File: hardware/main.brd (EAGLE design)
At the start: 95.2 x 80.4 mm, 100 parts, among them IC1 MPU-6050, IC2 TB6612FNG, M1 MOTOR_MOUNT_V2, M2 LED_MOUNT, M3 LED_MOUNT, M4 LED_MOUNT, M5 LED_MOUNT, M6 LED_MOUNT, M7 LED_MOUNT, Q7 IRLML2244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

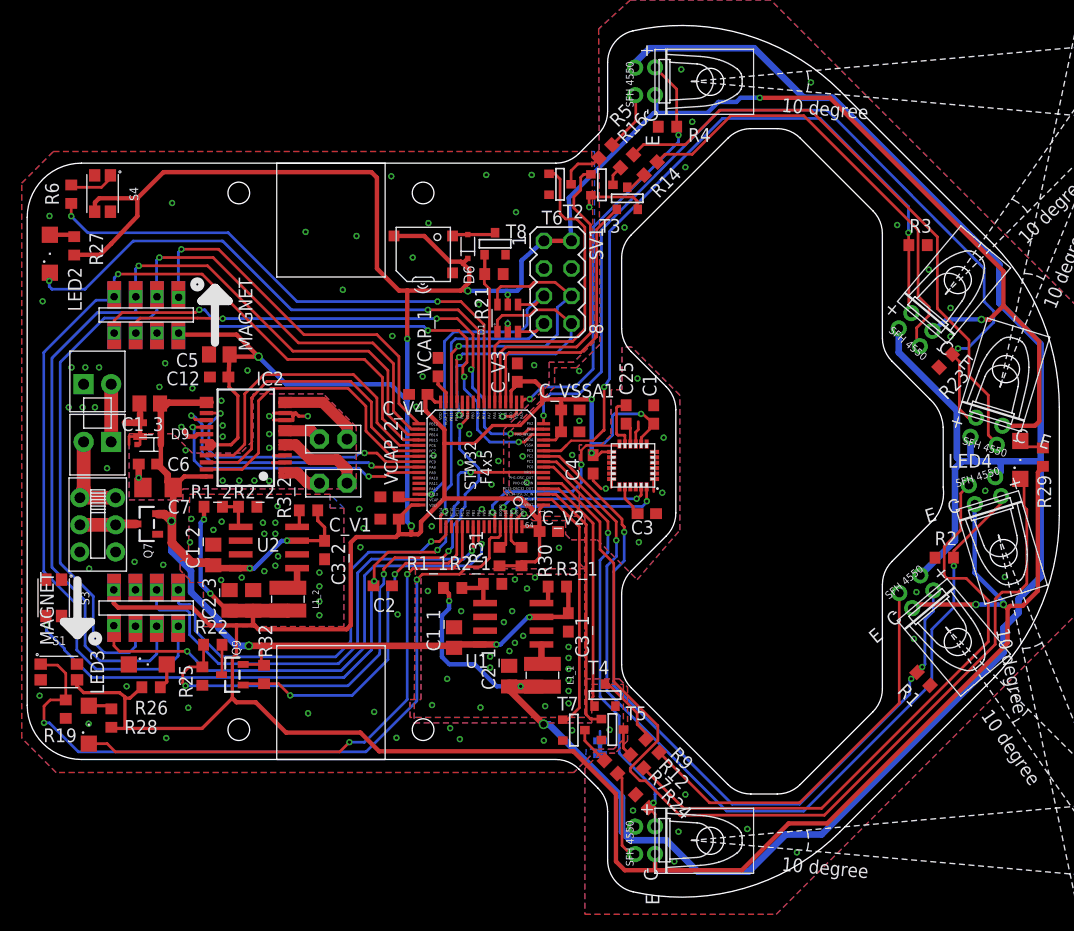
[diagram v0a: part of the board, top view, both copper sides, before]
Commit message: fixed boot0 button, buzzer footprint, togh matches 3d model
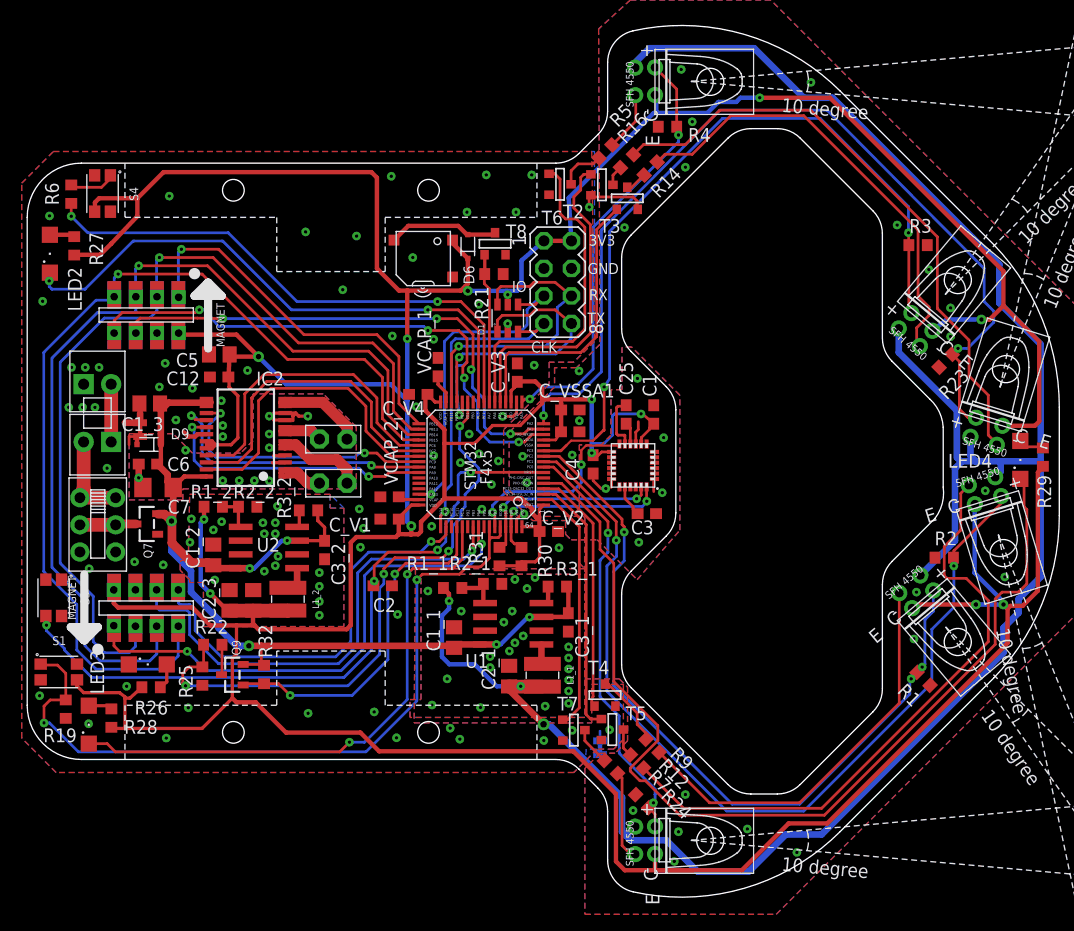
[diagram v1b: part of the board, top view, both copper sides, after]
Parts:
- moved SPK1 0.38 mm to (36.5, 18.7)
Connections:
- net +3V3: now also SPK1.+; no longer SPK1.-
- net BOOT0: now also U3.PB6
- net N$30: now also SPK1.-; no longer SPK1.+
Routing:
- net N$30: track 4.05 -> 10.3 mm
- net +3V3: track 527.2 -> 521.6 mm
- net BOOT0: track 68.7 -> 69.9 mm
- net GND: track 35.9 -> 35.3 mm, vias 111 -> 110
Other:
- board text added: "3V3"
- board text added: "CLK"
- board text added: "GND"
- board text added: "IO"
- board text added: "RX"
- board text added: "TX"

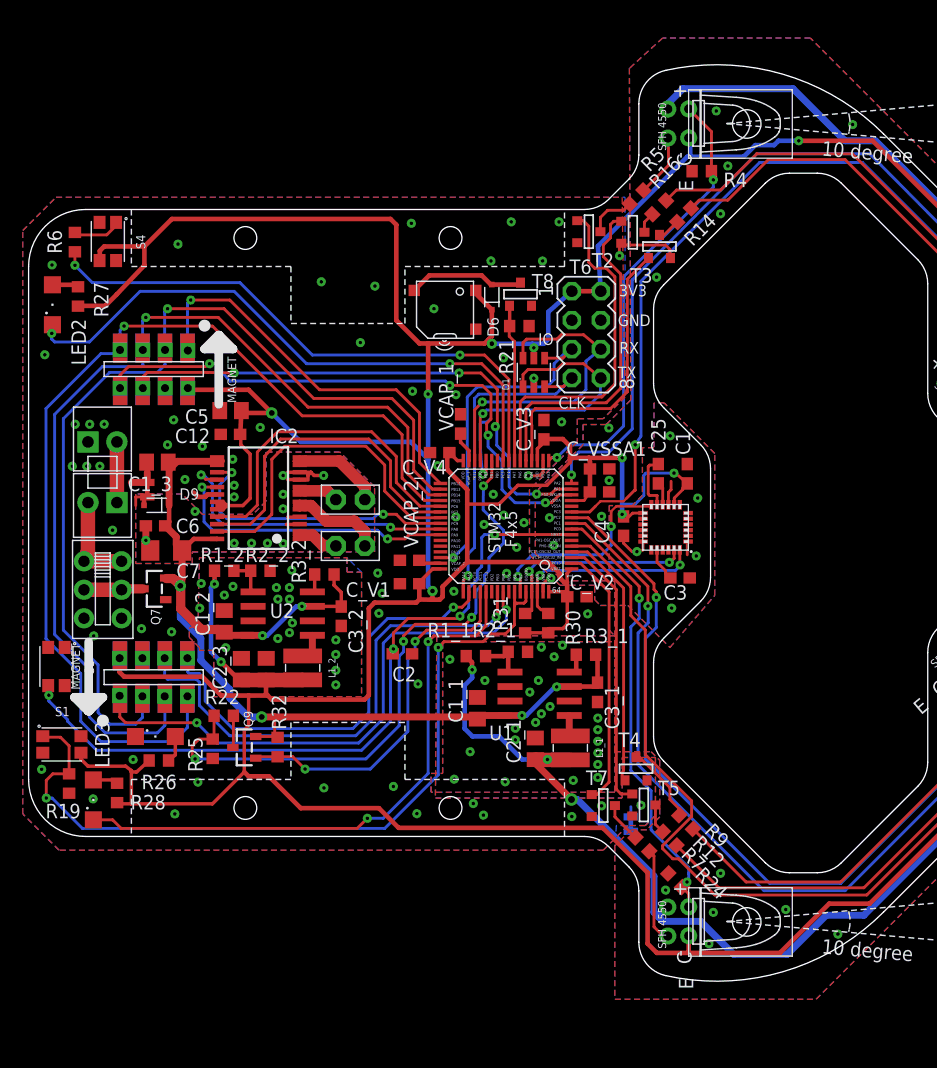
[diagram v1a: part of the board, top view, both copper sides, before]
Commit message: added mosfet pulldowns (IR leds), PB2 pulldown
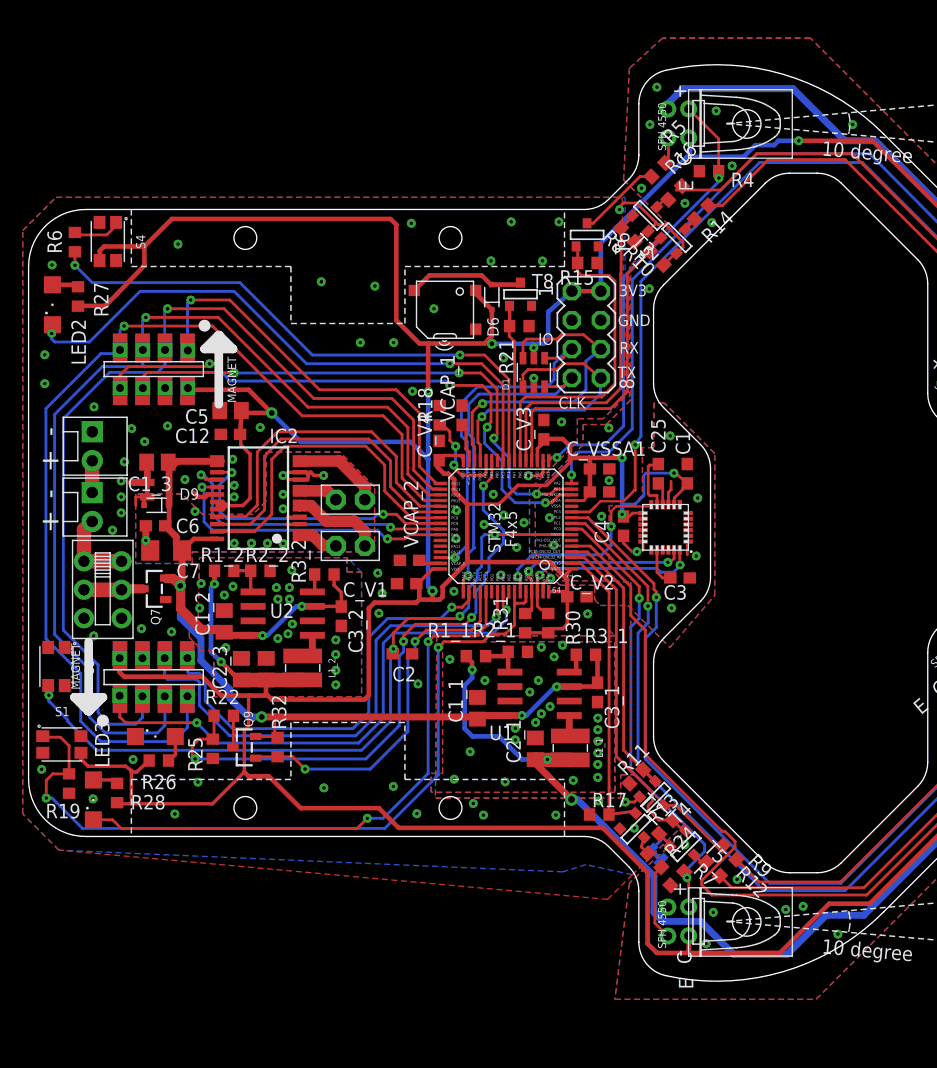
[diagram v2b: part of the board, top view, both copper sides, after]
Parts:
- added R10, R11, R13, R15, R17, R18, R8: 10k, rcl:R0603
- moved T5 5.19 mm to (57.7, -28.4), turned to 45 degrees
- moved R12 4.65 mm to (60.0, -30.4)
- moved R9 4.65 mm to (61.5, -28.9)
- moved T7 3.51 mm to (53.3, -26.9), turned to 45 degrees
- moved PT1 3.50 mm to (55.0, -29.1), turned to 135 degrees
- moved R5 3.07 mm to (55.2, 31.0)
- moved T4 3.02 mm to (55.0, -24.1), turned to 45 degrees
- moved JP1 2.34 mm to (5.58, 2.67), turned to 270 degrees
- moved T2 2.05 mm to (54.4, 27.0), turned to 135 degrees
- moved R16 1.89 mm to (56.7, 29.0)
- moved R7 1.76 mm to (54.9, -29.6)
- moved T3 1.70 mm to (56.9, 25.0), turned to 135 degrees
- moved R14 1.55 mm to (59.0, 27.3)
- moved JP2 0.97 mm to (5.59, 8.00), turned to 270 degrees
- moved VCAP_1 0.77 mm to (38.0, 9.45)
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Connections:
- new net N$3: R18.1, U3.PB2
- net D_L: now also R10.2
- net D_LF: now also R15.2
- net D_LS: now also R8.2
- net D_R: now also R11.2
- net D_RF: now also R17.2
- net D_RS: now also R13.2
- net GND: now also R10.1, R11.1, R13.1, R15.1, R17.1, R18.2, R8.1; no longer U3.PB2
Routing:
- net N$3: track 0.00 -> 8.78 mm, vias 0 -> 2
- net D_RS: track 24.4 -> 29.9 mm
- net N$8: track 57.8 -> 52.9 mm
- net N$6: track 38.0 -> 33.1 mm
- net GND: track 35.3 -> 39.8 mm
- net D_RF: track 23.0 -> 26.2 mm
- net N$4: track 4.43 -> 7.52 mm
- net N$2: track 5.56 -> 2.82 mm
- net N$19: track 5.32 -> 2.80 mm
- net D_L: track 25.9 -> 28.1 mm
- net N$5: track 3.55 -> 1.69 mm
- net D_LF: track 30.7 -> 29.0 mm
- net N$10: track 41.9 -> 40.3 mm
- net N$1: track 8.35 -> 6.75 mm
- net N$46: track 8.52 -> 7.09 mm
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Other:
- board text added: "+"
- board text added: "-"
- board text added: "RevB 2018.04"
- board text removed: "2017"

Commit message: fixed silkcreen covering pads
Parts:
- IC1: device invensense:QFN.24.4X4 -> micromouse:QFN.24.4X4
- SPK1: device adafruit:SMT-0540-S-R -> micromouse:SMT-0540-S-R
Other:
- board text added: "ON"

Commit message: more pcb fixes
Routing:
- net ENCR_A: track 38.8 -> 41.1 mm
- net ENCL_A: track 51.6 -> 53.1 mm
- net +3V3: track 522.2 -> 523.7 mm
- net N$12: track 55.3 -> 54.4 mm
- net ENCR_B: track 44.7 -> 45.6 mm
- net GND: track 39.8 -> 39.1 mm, vias 110 -> 111

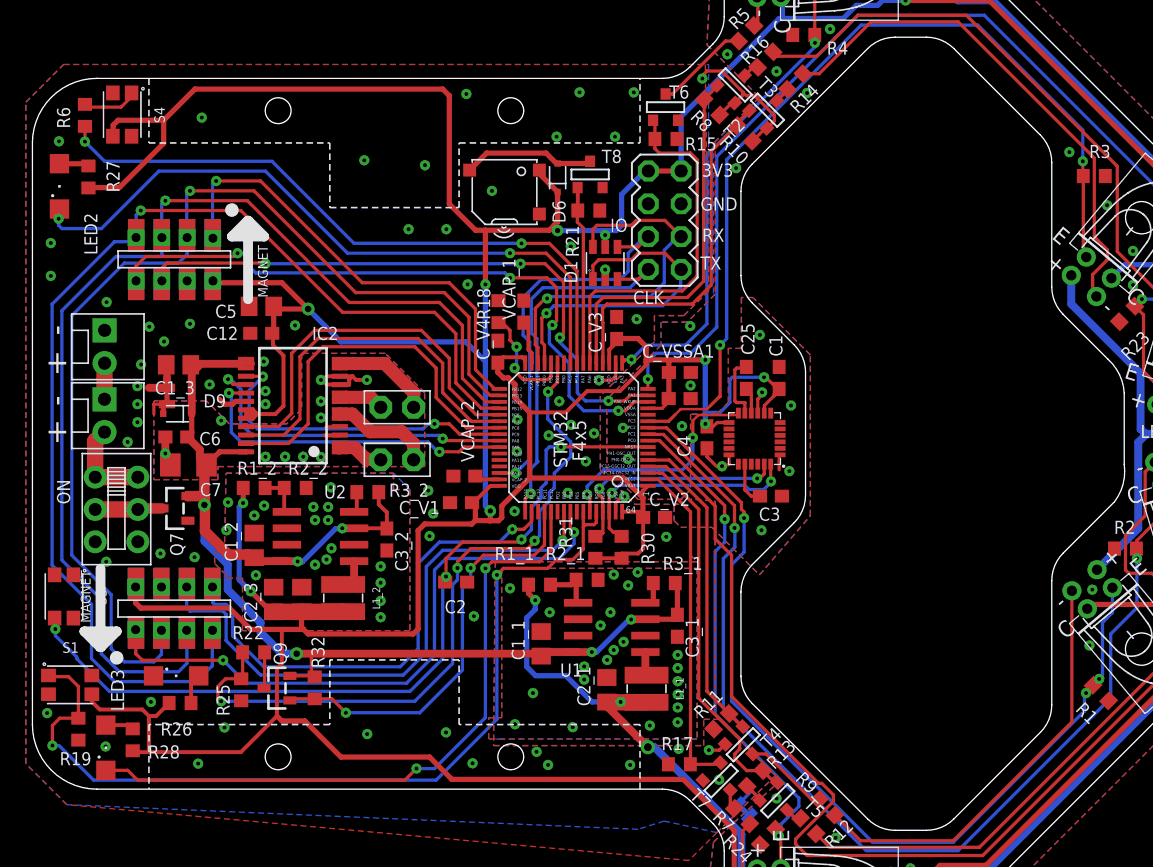
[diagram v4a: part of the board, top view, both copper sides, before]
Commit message: pcb matches the 3d model
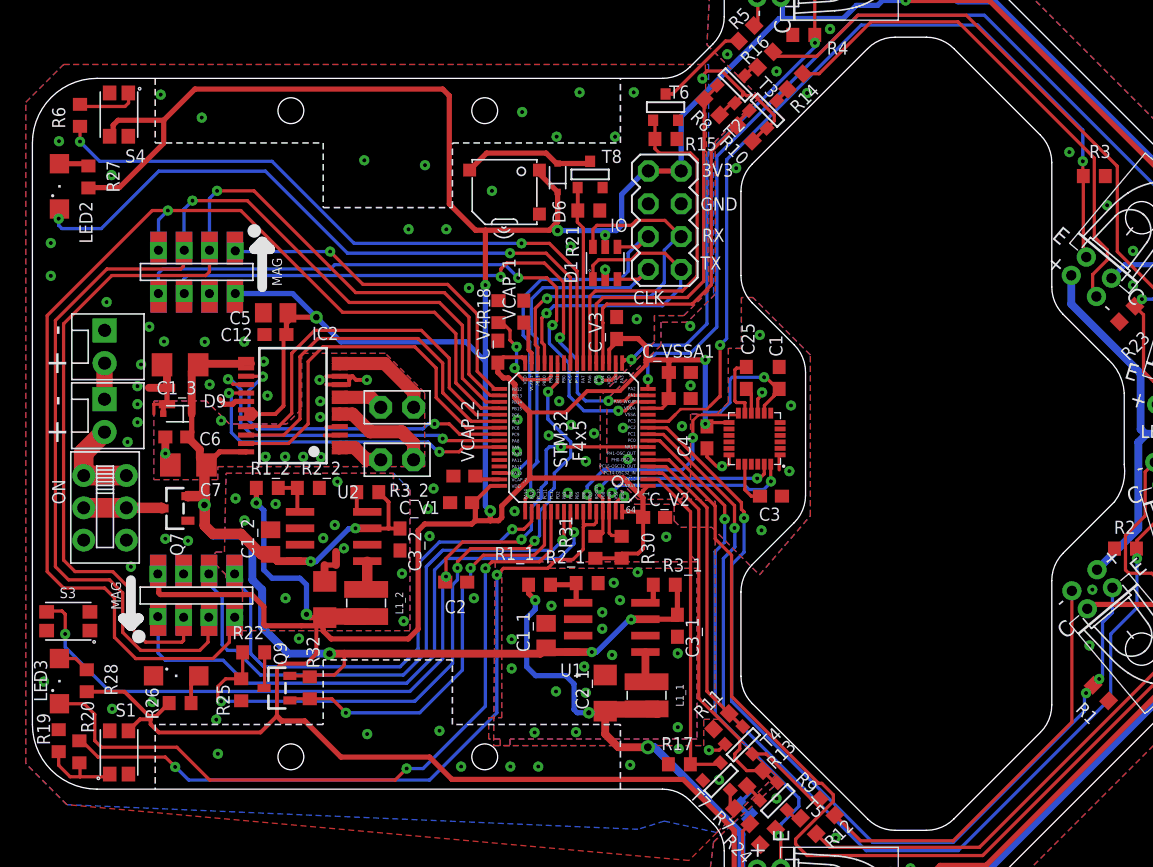
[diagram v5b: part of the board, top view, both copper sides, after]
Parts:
- removed C2_3: 10u, rcl:C0805
- added R20: 4,7k, rcl:R0603
- C1_3, C2_1, C2_2: device rcl:C0805 -> rcl:C1206
- moved S1 6.46 mm to (6.71, -24.7), turned to 90 degrees
- moved LED3 6.28 mm to (2.09, -19.1)
- moved R28 5.79 mm to (4.21, -19.1)
- moved U$10 1.99 mm to (12.7, -12.5)
- moved U$9 1.99 mm to (12.7, 12.5)
- moved S3 1.95 mm to (2.78, -14.5), turned to 180 degrees
- moved L1_2 1.82 mm to (25.8, -13.1)
- moved C2_2 1.78 mm to (22.6, -12.8)
- moved R19 1.76 mm to (2.03, -23.7), turned to 270 degrees
- moved C1_2 1.30 mm to (18.4, -8.38)
- moved C5 1.21 mm to (18.8, 9.36)
- moved C12 1.10 mm to (18.8, 7.68)
- moved R2_2 1.02 mm to (21.4, -4.19)
- moved C3_2 1.02 mm to (28.4, -8.18)
- moved R1_2 1.02 mm to (18.2, -4.19)
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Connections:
- new net ASDF: R19.2, R20.1, S1.1
- net +3V3: no longer C2_3.1
- net BOOT0: now also R20.2; no longer R19.2, S1.1
- net GND: no longer C2_3.2
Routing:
- net BOOT0: track 69.9 -> 58.8 mm
- net SPI2_CS1: track 35.7 -> 27.5 mm
- net ASDF: track 0.00 -> 6.56 mm
- net LED3: track 52.5 -> 58.3 mm
- net GND: track 39.1 -> 42.2 mm, vias 111 -> 100
- net +7V: track 98.0 -> 101.1 mm
- net VCC: track 203.4 -> 206.4 mm
- net ENCL_A: track 53.1 -> 50.2 mm, vias 4 -> 3
- net ENCR_A: track 41.1 -> 38.4 mm
- net ENCR_B: track 45.6 -> 43.9 mm
- net RST: track 64.7 -> 66.2 mm
- net +3V3: track 523.7 -> 522.2 mm
- net SPI2_SCK: track 82.8 -> 84.2 mm
- net N$43: track 5.18 -> 6.08 mm
- net ENCL_B: track 48.4 -> 47.6 mm, vias 4 -> 3
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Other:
- board text added: "RevB 2018.05"
- board text removed: "RevB 2018.04"

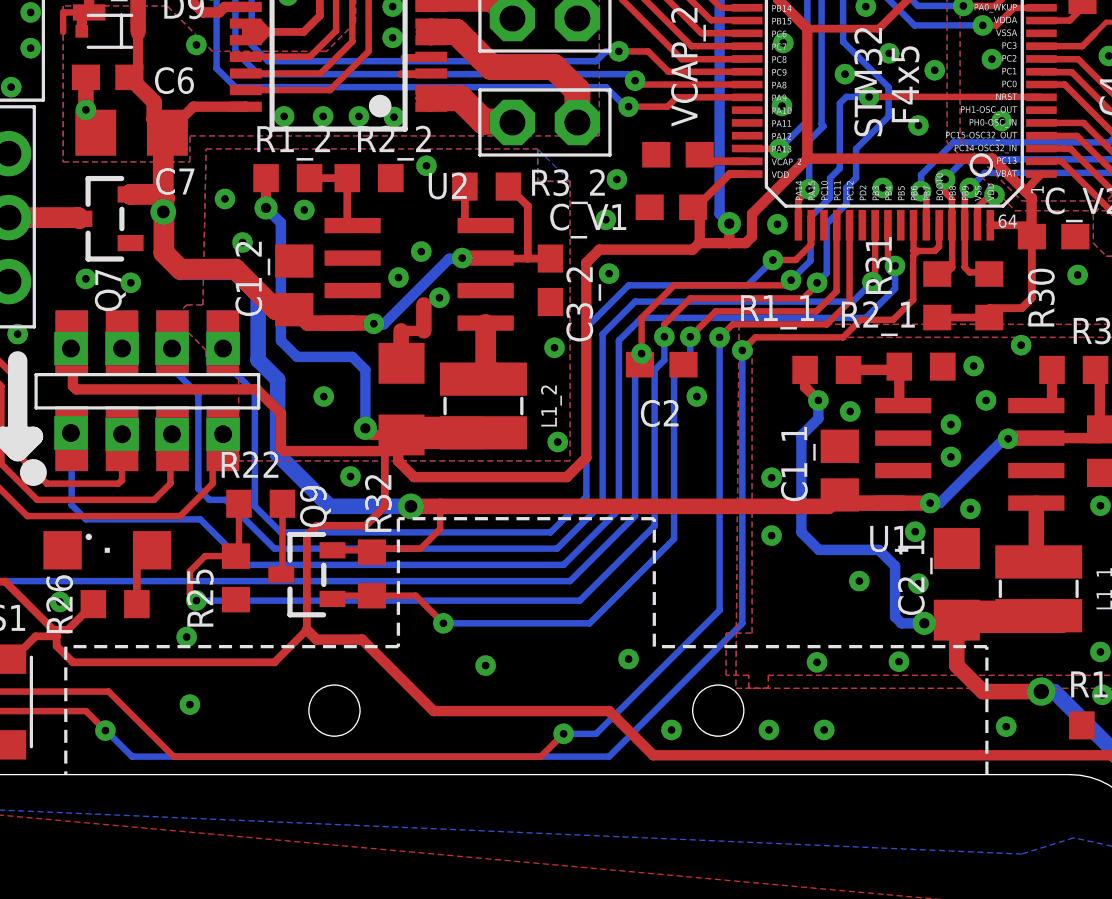
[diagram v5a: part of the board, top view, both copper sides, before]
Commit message: fixed gnd connection for C1_1 and C1_2 caps (dc converter)
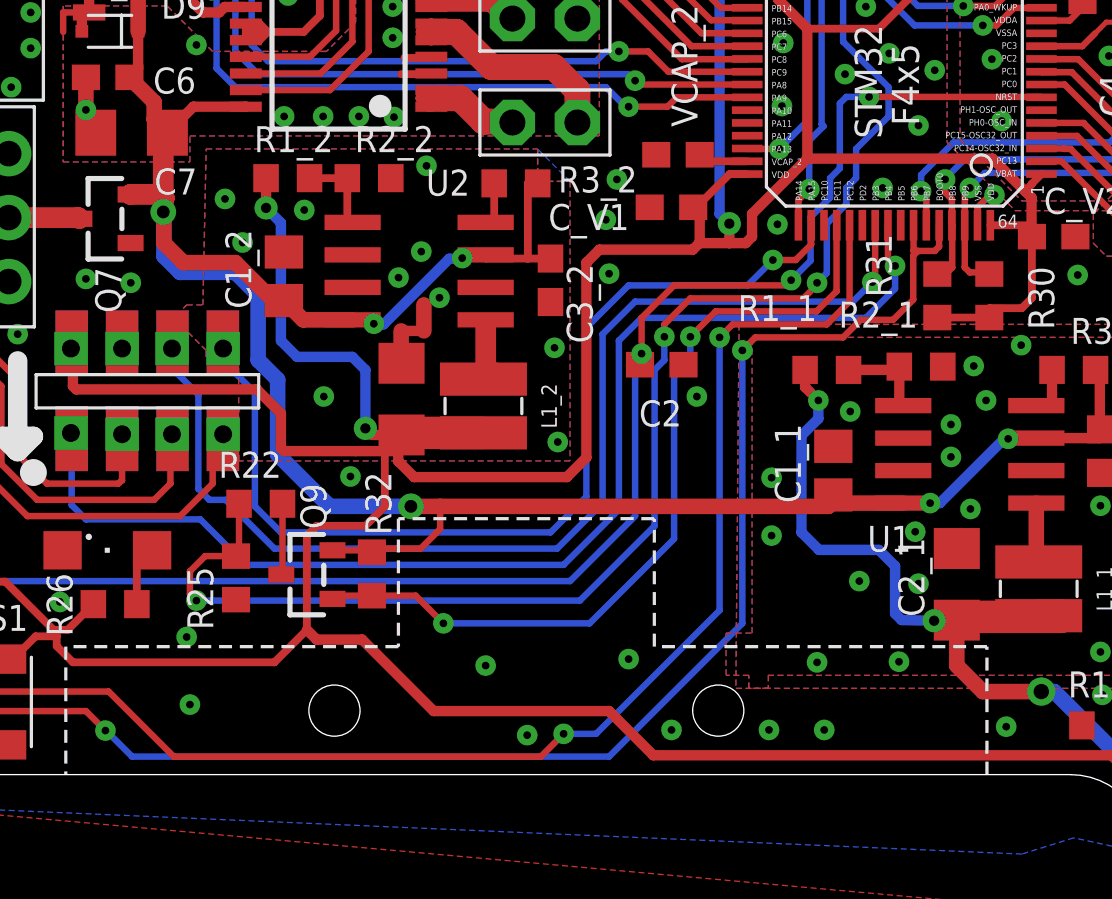
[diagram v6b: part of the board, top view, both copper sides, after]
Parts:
- moved R3_2 1.15 mm to (27.1, -4.39)
- moved C1_2 0.54 mm to (18.0, -8.03)
- moved C1_1 0.25 mm to (39.5, -15.6)
- moved U2 0.13 mm to (23.3, -7.82)
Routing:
- net GND: vias 100 -> 101
